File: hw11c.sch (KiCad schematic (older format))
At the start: 77 parts, among them Q1 KX-7_12MHZ, SW1 BUTT1, SW2 BUTT2, X1 ~RESET, X10 PIO2.8, X11 PIO1.4, X12 ADC3, X13 PIO0.8, X14 PIO0.9, X15 MAT0, X16 PIO0.6, X17 PIO0.7, X2 SWCLK, X3 SWDIO, X4 SSEL1, X5 SCK1, X6 MISO1, X7 MOSI1, X8 PIO2.6, X9 PIO2.7

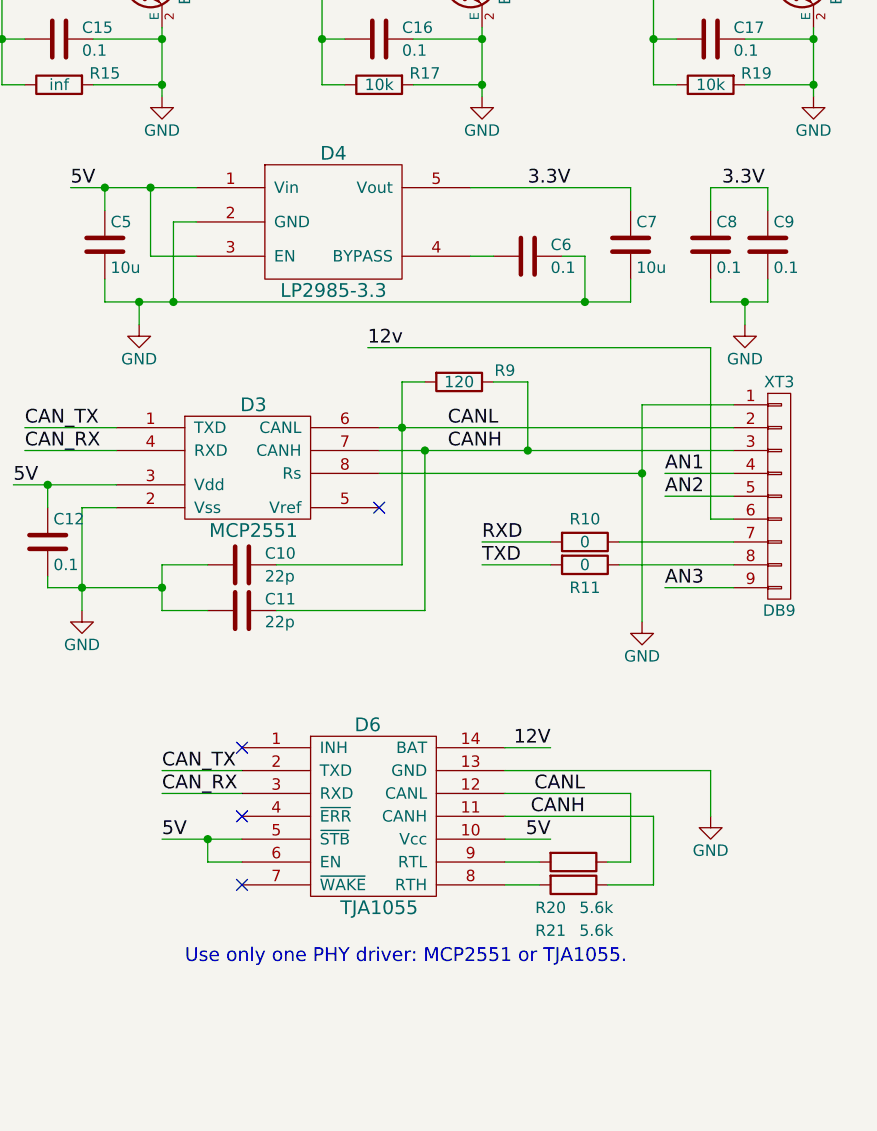
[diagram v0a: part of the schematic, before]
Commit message: Fix silk layer. Add wiki links.
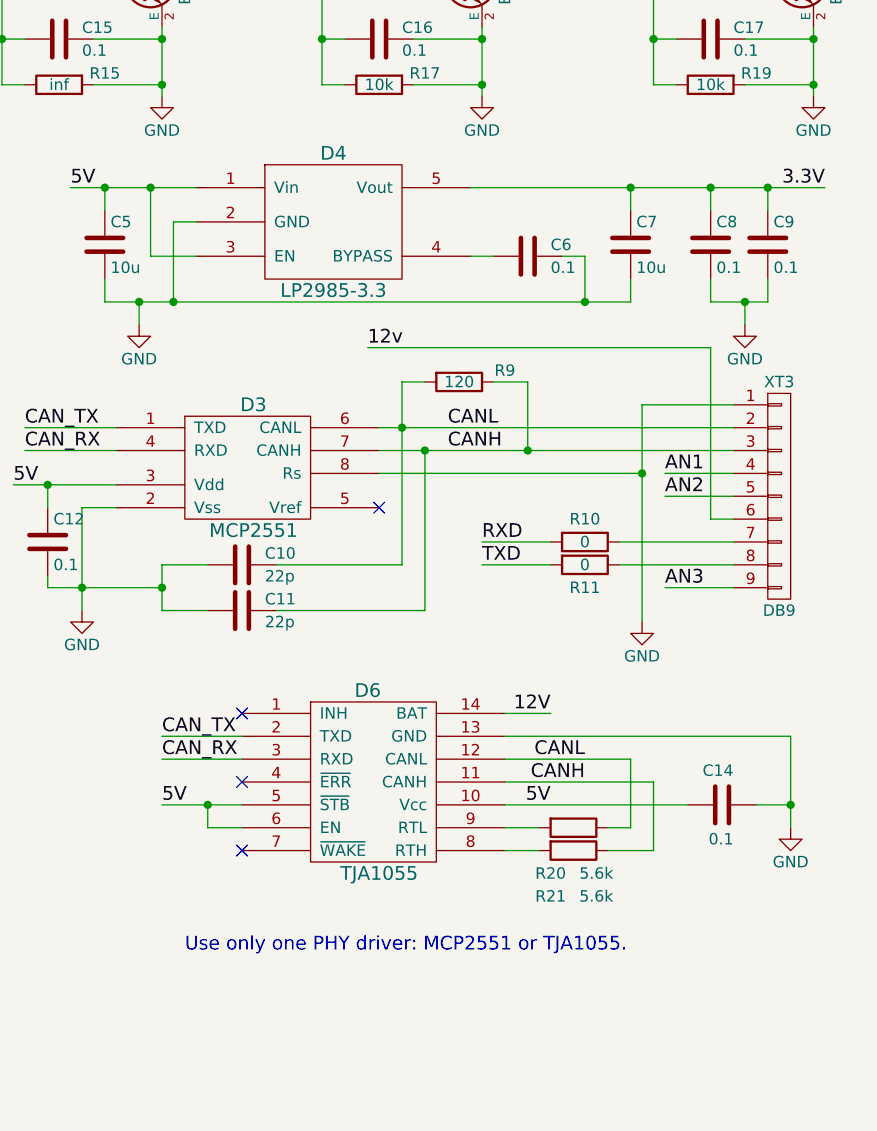
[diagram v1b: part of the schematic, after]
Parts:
- added C14: 0.1, libs:C_0603, symbol C
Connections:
- net 5V: now also C14.1
- net GND: now also C14.2
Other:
- moved on the sheet: D6, R20, R21
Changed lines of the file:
@@
 Text Label 4450 1450 2    60   ~ 0
-3.3V
-Text Label 9100 2300 0    60   ~ 0
 3.3V
 $Comp
@@
 	1    0    0    -1
 $EndComp
-Text Label 9950 2300 0    60   ~ 0
+Text Label 10400 2300 2    60   ~ 0
 3.3V
 Text Label 2600 3650 0    60   ~ 0
@@
 L TJA1055 D6
 U 1 1 5A7858B3
-P 8400 5050
-F 0 "D6" H 8400 5450 60  0000 C CNN
-F 1 "TJA1055" H 8450 4650 60  0000 C CNN
-F 2 "libs:SOIC-14_N" H 8350 4800 60  0001 C CNN
-F 3 "" H 8350 4800 60  0000 C CNN
-	1    8400 5050
-	1    0    0    -1
-$EndComp
-Text Label 7500 4850 0    60   ~ 0
+P 8400 4900
+F 0 "D6" H 8400 5300 60  0000 C CNN
+F 1 "TJA1055" H 8450 4500 60  0000 C CNN
+F 2 "libs:SOIC-14_N" H 8350 4650 60  0001 C CNN
+F 3 "" H 8350 4650 60  0000 C CNN
+	1    8400 4900
+	1    0    0    -1
+$EndComp
+Text Label 7500 4700 0    60   ~ 0
 CAN_TX
-Text Label 7500 4950 0    60   ~ 0
+Text Label 7500 4800 0    60   ~ 0
 CAN_RX
-Text Label 9350 4950 2    60   ~ 0
+Text Label 9350 4800 2    60   ~ 0
 CANL
-Text Label 9350 5050 2    60   ~ 0
+Text Label 9350 4900 2    60   ~ 0
 CANH
 $Comp
 L R R21
 U 1 1 5A7894A7
-P 9300 5350
-F 0 "R21" V 9500 5250 50  0000 C CNN
-F 1 "5.6k" V 9500 5450 50  0000 C CNN
-F 2 "libs:R_0603" V 9230 5350 50  0001 C CNN
-F 3 "" H 9300 5350 50  0000 C CNN
-	1    9300 5350
+P 9300 5200
+F 0 "R21" V 9500 5100 50  0000 C CNN
+F 1 "5.6k" V 9500 5300 50  0000 C CNN
+F 2 "libs:R_0603" V 9230 5200 50  0001 C CNN
+F 3 "" H 9300 5200 50  0000 C CNN
+	1    9300 5200
 	0    1    1    0
 $EndComp
@@
 L R R20
 U 1 1 5A78959E
-P 9300 5250
-F 0 "R20" V 9500 5150 50  0000 C CNN
-F 1 "5.6k" V 9500 5350 50  0000 C CNN
-F 2 "libs:R_0603" V 9230 5250 50  0001 C CNN
-F 3 "" H 9300 5250 50  0000 C CNN
-	1    9300 5250
-	0    1    1    0
-$EndComp
-Text Label 9200 5150 2    60   ~ 0
+P 9300 5100
+F 0 "R20" V 9500 5000 50  0000 C CNN
+F 1 "5.6k" V 9500 5200 50  0000 C CNN
+F 2 "libs:R_0603" V 9230 5100 50  0001 C CNN
+F 3 "" H 9300 5100 50  0000 C CNN
+	1    9300 5100
+	0    1    1    0
+$EndComp
+Text Label 9200 5000 2    60   ~ 0
 5V
 $Comp
 L GND #PWR019
 U 1 1 5A78A1CB
-P 9900 5050
-F 0 "#PWR019" H 9900 4800 50  0001 C CNN
-F 1 "GND" H 9900 4900 50  0000 C CNN
-F 2 "" H 9900 5050 50  0000 C CNN
-F 3 "" H 9900 5050 50  0000 C CNN
-	1    9900 5050
-	1    0    0    -1
-$EndComp
-Text Label 9200 4750 2    60   ~ 0
+P 10250 5100
+F 0 "#PWR019" H 10250 4850 50  0001 C CNN
+F 1 "GND" H 10250 4950 50  0000 C CNN
+F 2 "" H 10250 5100 50  0000 C CNN
+F 3 "" H 10250 5100 50  0000 C CNN
+	1    10250 5100
+	1    0    0    -1
+$EndComp
+Text Label 9200 4600 2    60   ~ 0
 12V
-Text Label 7500 5150 0    60   ~ 0
+Text Label 7500 5000 0    60   ~ 0
 5V
-NoConn ~ 7850 4750
-NoConn ~ 7850 5050
-NoConn ~ 7850 5350
-Text Notes 7600 5700 0    60   ~ 0
+NoConn ~ 7850 4600
+NoConn ~ 7850 4900
+NoConn ~ 7850 5200
+Text Notes 7600 5650 0    60   ~ 0
 Use only one PHY driver: MCP2551 or TJA1055.
 $Comp
@@
 	10150 2300 10150 2400
 Wire Wire Line
-	9900 2300 10150 2300
+	8850 2300 10400 2300
 Wire Wire Line
 	9900 2400 9900 2300
@@
 Wire Wire Line
 	9550 2300 9550 2400
-Wire Wire Line
-	8850 2300 9550 2300
 Connection ~ 7400 2800
 Wire Wire Line
@@
 	2950 2350 2700 2350
 Wire Wire Line
-	7500 4850 7850 4850
-Wire Wire Line
-	7500 4950 7850 4950
-Wire Wire Line
-	9000 4950 9550 4950
-Wire Wire Line
-	9000 5050 9650 5050
-Wire Wire Line
-	9000 5250 9150 5250
-Wire Wire Line
-	9450 5250 9550 5250
-Wire Wire Line
-	9550 5250 9550 4950
-Wire Wire Line
-	9650 5050 9650 5350
-Wire Wire Line
-	9650 5350 9450 5350
-Wire Wire Line
-	9150 5350 9000 5350
-Wire Wire Line
-	9200 5150 9000 5150
-Wire Wire Line
-	9900 5050 9900 4850
-Wire Wire Line
-	9900 4850 9000 4850
-Wire Wire Line
-	9000 4750 9200 4750
-Wire Wire Line
-	7500 5150 7850 5150
-Wire Wire Line
-	7850 5250 7700 5250
-Wire Wire Line
-	7700 5250 7700 5150
-Connection ~ 7700 5150
+	7500 4700 7850 4700
+Wire Wire Line
+	7500 4800 7850 4800
+Wire Wire Line
+	9000 4800 9550 4800
+Wire Wire Line
+	9000 4900 9650 4900
+Wire Wire Line
+	9000 5100 9150 5100
+Wire Wire Line
+	9450 5100 9550 5100
+Wire Wire Line
+	9550 5100 9550 4800
+Wire Wire Line
+	9650 4900 9650 5200
+Wire Wire Line
+	9650 5200 9450 5200
+Wire Wire Line
+	9150 5200 9000 5200
+Wire Wire Line
+	9000 5000 9800 5000
+Wire Wire Line
+	9000 4700 10250 4700
+Wire Wire Line
+	9000 4600 9200 4600
+Wire Wire Line
+	7500 5000 7850 5000
+Wire Wire Line
+	7850 5100 7700 5100
+Wire Wire Line
+	7700 5100 7700 5000
+Connection ~ 7700 5000
 Connection ~ 7500 1650
 Wire Wire Line
@@
 Connection ~ 10350 1100
 Connection ~ 10350 1650
+Connection ~ 9550 2300
+Connection ~ 9900 2300
+Connection ~ 10150 2300
+$Comp
+L C C14
+U 1 1 5A8BFDF8
+P 9950 5000
+F 0 "C14" V 10100 4950 50  0000 L CNN
+F 1 "0.1" V 9800 4950 50  0000 L CNN
+F 2 "libs:C_0603" H 9988 4850 50  0001 C CNN
+F 3 "" H 9950 5000 50  0000 C CNN
+	1    9950 5000
+	0    -1   -1   0
+$EndComp
+Wire Wire Line
+	10250 4700 10250 5100
+Wire Wire Line
+	10250 5000 10100 5000
+Connection ~ 10250 5000
 $EndSCHEMATC

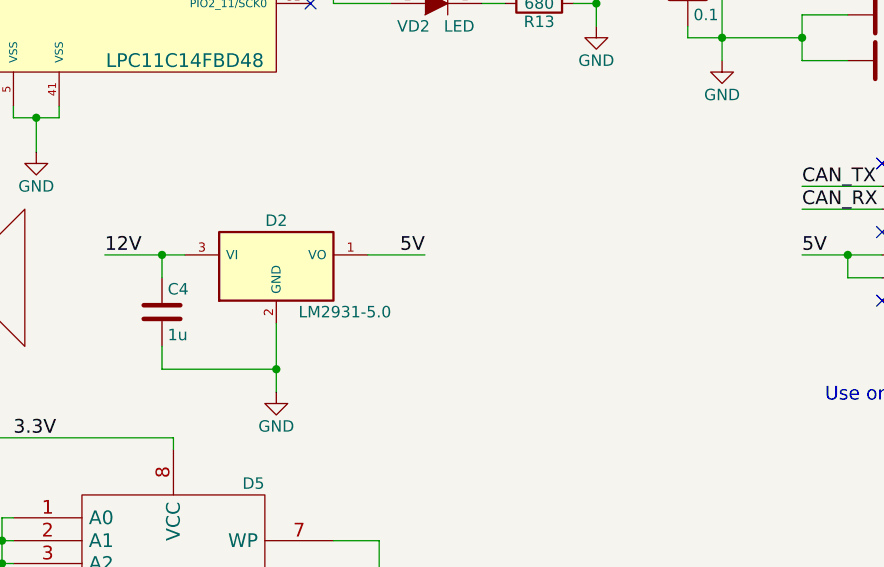
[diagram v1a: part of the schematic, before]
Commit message: Fix SO-14 case for TJA-1055.
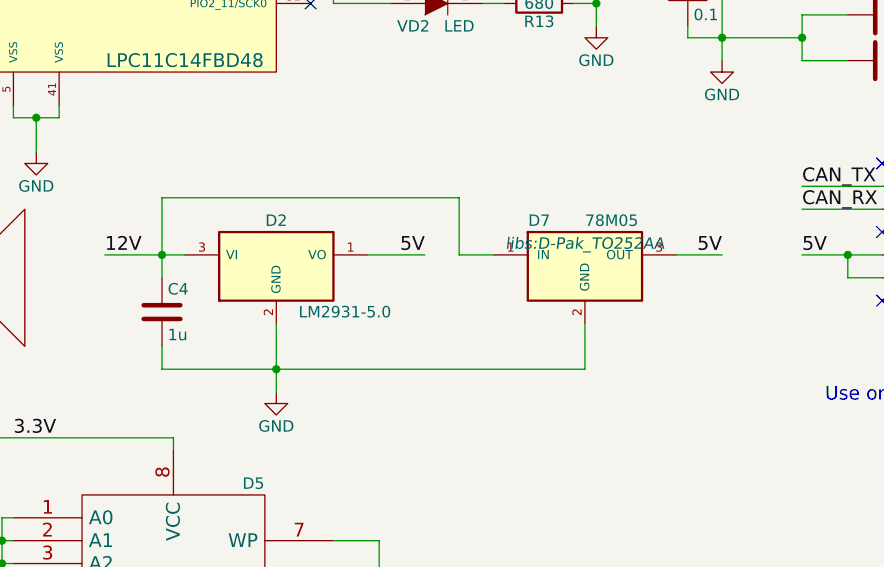
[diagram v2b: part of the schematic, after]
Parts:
- added D7: 78M05, libs:D-Pak_TO252AA, symbol MC78M05CDT
- D6: footprint libs:SOIC-14_N -> libs:SOIC-14_3.9x8.7mm_Pitch1.27mm
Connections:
- net 12V: now also D7.1 (IN)
- net 5V: now also D7.3 (OUT)
- net GND: now also D7.2 (GND)
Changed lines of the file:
@@
 F 0 "D6" H 8400 5300 60  0000 C CNN
 F 1 "TJA1055" H 8450 4500 60  0000 C CNN
-F 2 "libs:SOIC-14_N" H 8350 4650 60  0001 C CNN
+F 2 "libs:SOIC-14_3.9x8.7mm_Pitch1.27mm" H 8350 4650 60  0001 C CNN
 F 3 "" H 8350 4650 60  0000 C CNN
 	1    8400 4900
@@
 	2100 6250 2100 6750
 Wire Wire Line
-	4700 5500 5200 5500
-Wire Wire Line
 	5650 1850 5350 1850
 Wire Wire Line
@@
 	4450 5000 4800 5000
 Wire Wire Line
-	4700 5100 4700 5000
+	4700 4750 4700 5100
 Wire Wire Line
 	2100 6750 1700 6750
@@
 	10250 5000 10100 5000
 Connection ~ 10250 5000
+$Comp
+L MC78M05CDT D7
+U 1 1 5ACDE29A
+P 6550 5050
+F 0 "D7" H 6350 5250 50  0000 C CNN
+F 1 "78M05" H 6550 5250 50  0000 L CNN
+F 2 "libs:D-Pak_TO252AA" H 6550 5150 50  0000 C CIN
+F 3 "" H 6550 5050 50  0000 C CNN
+	1    6550 5050
+	1    0    0    -1
+$EndComp
+Wire Wire Line
+	4700 4750 6000 4750
+Wire Wire Line
+	6000 4750 6000 5000
+Wire Wire Line
+	6000 5000 6150 5000
+Wire Wire Line
+	6550 5300 6550 5500
+Wire Wire Line
+	6550 5500 4700 5500
+Text Label 7150 5000 2    60   ~ 0
+5V
+Wire Wire Line
+	7150 5000 6950 5000
 $EndSCHEMATC

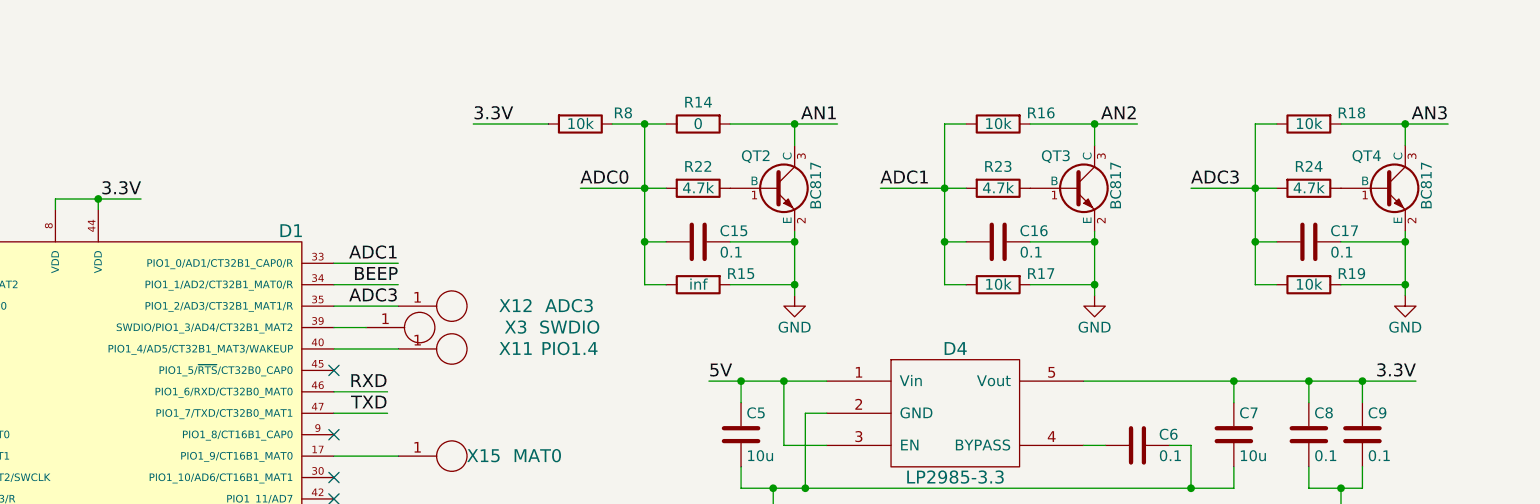
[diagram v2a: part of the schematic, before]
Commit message: Add resistive divider on ADC5 (AIN4) for system voltage measurement. Add reference voltage for AIN2. Add information on scheme.
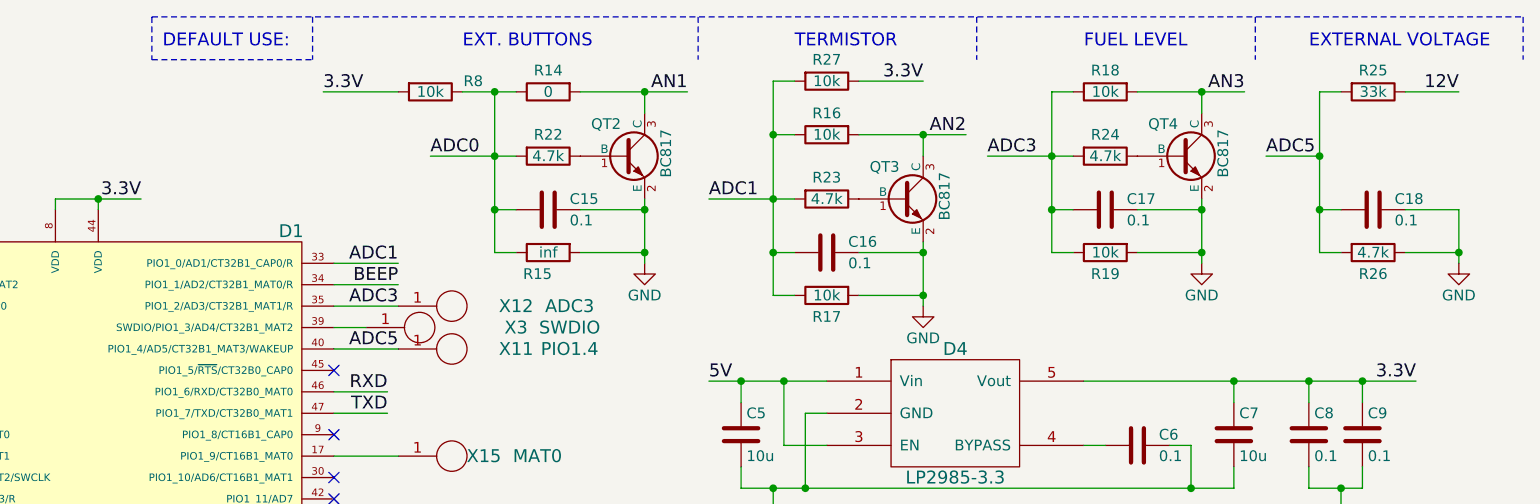
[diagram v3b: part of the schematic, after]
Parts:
- added C18: 0.1, libs:C_0603, symbol C
- added R25: 33k, libs:R_0603, symbol R
- added R26: 4.7k, libs:R_0603, symbol R
- added R27: 10k, libs:R_0603, symbol R
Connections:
- net 12V: now also R25.1
- net 3.3V: now also R27.1
- net ADC1: now also R27.2
- net GND: now also C18.1, R26.1
- net ADC5: now reaches D1.40 (PIO1_4/AD5/CT32B1_MAT3/WAKEUP), X11.1
- net ADC5: now also C18.2, R25.2, R26.2
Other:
- note added: "DEFAULT USE:"
- note added: "EXT. BUTTONS"
- note added: "EXTERNAL VOLTAGE"
- note added: "FUEL LEVEL"
- note added: "TERMISTOR"
- moved on the sheet: C15, C16, C17, QT2, QT3, QT4, R14, R15, R16, R17, R18, R19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

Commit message: Clear TODO.md. Fix capasitors on scheme.
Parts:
- C13, C14, C15, C16, C17, C18: symbol C -> C-RESCUE-hw11c
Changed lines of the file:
@@
 $EndComp
 $Comp
-L C C13
+L C-RESCUE-hw11c C13
 U 1 1 5714CCE8
 P 3750 6400
@@
 AN2
 $Comp
-L C C16
+L C-RESCUE-hw11c C16
 U 1 1 57B37732
 P 7650 1700
@@
 AN3
 $Comp
-L C C17
+L C-RESCUE-hw11c C17
 U 1 1 57B3CAF2
 P 8950 1500
@@
 AN1
 $Comp
-L C C15
+L C-RESCUE-hw11c C15
 U 1 1 57B3CC50
 P 6350 1500
@@
 Connection ~ 10150 2300
 $Comp
-L C C14
+L C-RESCUE-hw11c C14
 U 1 1 5A8BFDF8
 P 9950 5000
@@
 F 0 "D7" H 6350 5250 50  0000 C CNN
 F 1 "78M05" H 6550 5250 50  0000 L CNN
-F 2 "libs:D-Pak_TO252AA" H 6550 5150 50  0000 C CIN
+F 2 "libs:D-Pak_TO252AA" H 6550 4750 50  0001 C CIN
 F 3 "" H 6550 5050 50  0000 C CNN
 	1    6550 5050
@@
 $EndComp
 $Comp
-L C C18
+L C-RESCUE-hw11c C18
 U 1 1 5B1B98B4
 P 10200 1500

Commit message: Add X18 pad.
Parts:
- added X18: ADC6, libs:PAD, symbol PAD
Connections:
- net at D1.30 (PIO1_10/AD6/CT16B1_MAT1): now also X18.1
- no-connect marks 14 -> 13
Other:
- note added: "EXT. BUTTONS (AN1)"
- note added: "FUEL LEVEL (AN3)"
- note added: "TERMISTOR (AN2)"
- note removed: "EXT. BUTTONS"
- note removed: "FUEL LEVEL"
- note removed: "TERMISTOR"
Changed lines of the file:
@@
 NoConn ~ 5350 2250
 NoConn ~ 5350 2550
-NoConn ~ 5350 2750
 NoConn ~ 5350 2850
 NoConn ~ 5350 3900
@@
 Wire Wire Line
 	10600 950  10350 950
-Text Notes 5950 750  0    60   ~ 0
-EXT. BUTTONS
+Text Notes 5700 750  0    60   ~ 0
+EXT. BUTTONS (AN1)
 $Comp
 L R R27
@@
 Wire Wire Line
 	8100 900  7800 900
-Text Notes 7500 750  0    60   ~ 0
-TERMISTOR
+Text Notes 7350 750  0    60   ~ 0
+TERMISTOR (AN2)
 Text Notes 9900 750  0    60   ~ 0
 EXTERNAL VOLTAGE
-Text Notes 8850 750  0    60   ~ 0
-FUEL LEVEL
+Text Notes 8600 750  0    60   ~ 0
+FUEL LEVEL (AN3)
 Text Notes 4550 750  0    60   ~ 0
 DEFAULT USE:
@@
 Wire Notes Line
 	10900 600  10900 800
+$Comp
+L PAD X18
+U 1 1 5B33AFBF
+P 5750 2750
+F 0 "X18" H 5450 2750 60  0000 C CNN
+F 1 "ADC6" H 5200 2750 60  0000 C CNN
+F 2 "libs:PAD" H 5750 2750 60  0001 C CNN
+F 3 "" H 5750 2750 60  0001 C CNN
+	1    5750 2750
+	-1   0    0    1
+$EndComp
+Wire Wire Line
+	5350 2750 5500 2750
 $EndSCHEMATC
